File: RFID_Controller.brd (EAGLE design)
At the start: 77 x 67 mm, 25 parts, among them IC1 74HC595N, K1 FTR-K1C, T1 BC547, T2 BC547

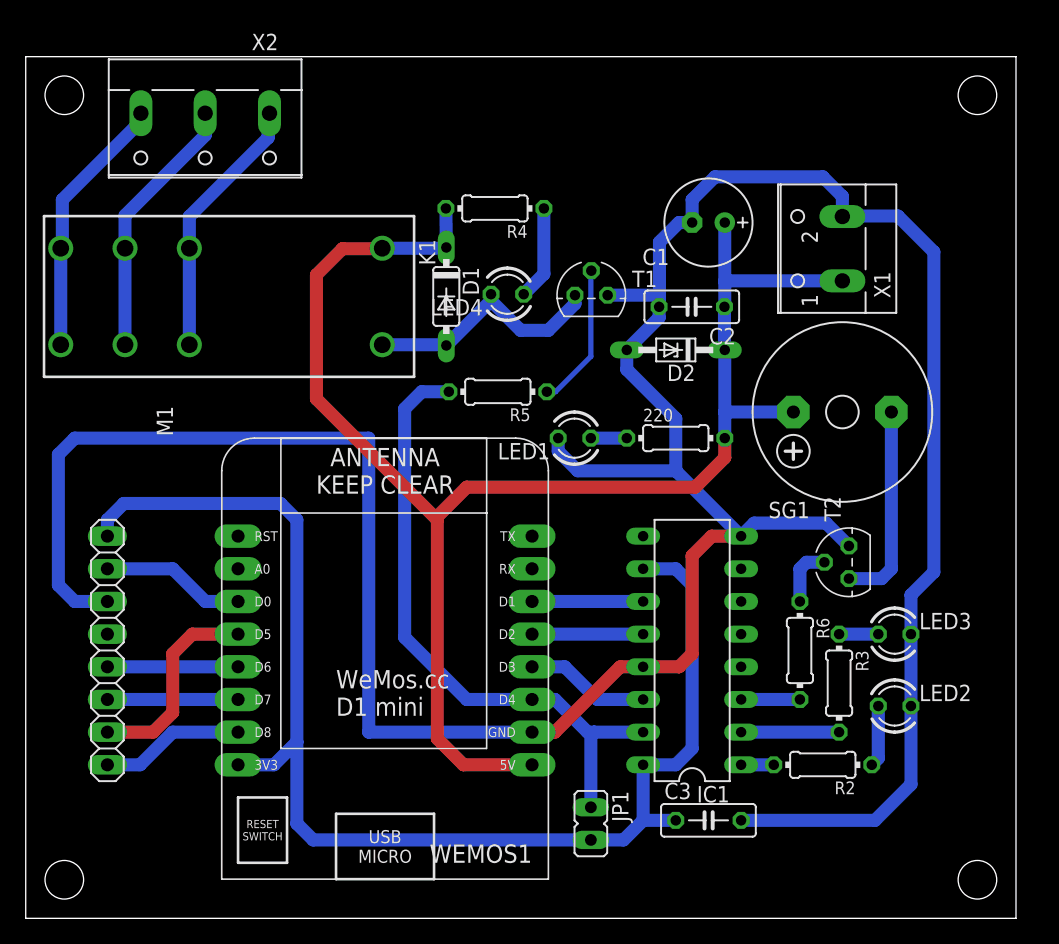
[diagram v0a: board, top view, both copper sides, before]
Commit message: -add: I2C Expander for more GPIOs -add: input for sabotage detection ( switch for enclosure cover ) -add: 2 more inputs for possible extensions -mod: additional resistor in pull-up path of relais transistor
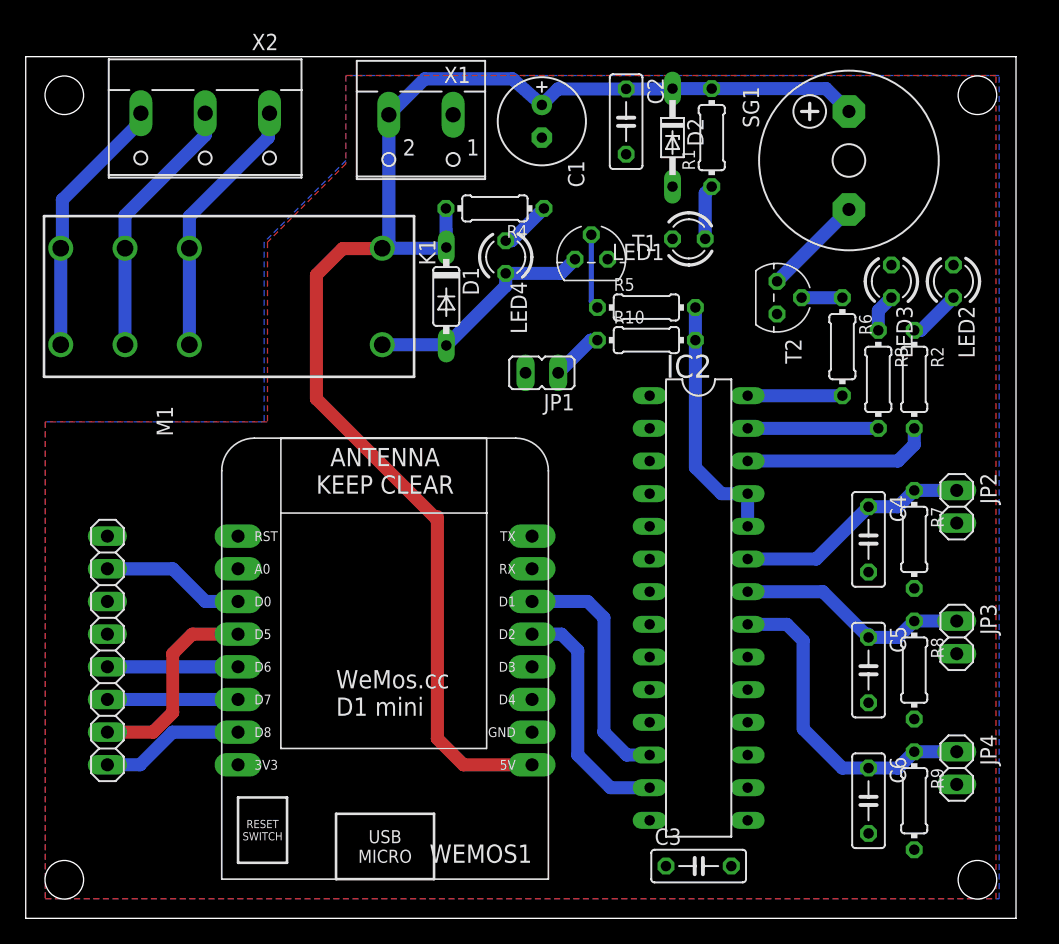
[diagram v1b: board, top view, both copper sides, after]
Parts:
- removed 220: (no value), rcl:0204/7
- removed IC1: 74HC595N, 74xx-eu:DIL16
- added C4, C5, C6: 100n, rcl:C050-025X075
- added IC2: MCP23017SP, microchip:DIL28-3
- added JP2, JP3, JP4: (no value), pinhead:1X02
- added R1: 220, rcl:0204/7
- added R10, R7, R8, R9: 10k, rcl:0204/7
- moved JP1 35.3 mm to (40.1, 42.4), turned to 90 degrees
- moved LED2 33.3 mm to (72.1, 49.5), turned to 270 degrees
- moved X1 32.8 mm to (30.7, 61.2), turned to 180 degrees
- moved R2 30.8 mm to (69.1, 41.9), turned to 270 degrees
- moved LED3 27.4 mm to (67.3, 49.5), turned to 270 degrees
- moved R6 23.9 mm to (63.5, 44.5)
- moved R3 23.8 mm to (66.3, 41.9)
- moved T2 21.3 mm to (58.4, 48.3), turned to 270 degrees
- moved SG1 19.6 mm to (64.0, 58.9), turned to 90 degrees
- moved LED1 17.9 mm to (51.6, 52.8)
- moved D2 16.5 mm to (50.3, 60.7), turned to 270 degrees
- moved C2 15.3 mm to (46.7, 62.0), turned to 270 degrees
- moved C1 15.2 mm to (40.1, 62.0), turned to 270 degrees
- moved R5 13.3 mm to (48.3, 47.5), turned to 0 degrees
- moved C3 3.64 mm to (52.3, 4.06)
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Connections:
- removed net CLK_595: IC1.11, WEMOS1.D1
- removed net SER: IC1.14, WEMOS1.D3
- removed net SET: IC1.12, WEMOS1.D2
- new net DK: C4.1, IC2.23, JP2.1, R7.1
- new net EX0: C5.1, IC2.22, JP3.1, R8.1
- new net EX1: C6.1, IC2.21, JP4.1, R9.1
- new net N$12: JP1.1, R10.1
- new net SCL: IC2.12, WEMOS1.D1
- new net SDA: IC2.13, WEMOS1.D2
- net 3V3: now also IC2.18, IC2.9, LED2.A, LED3.A, R7.2, R8.2, R9.2; no longer IC1.10, IC1.16
- net 5V: now also R1.2, X1.2; no longer 220.2, X1.1
- net BUZZ: now also IC2.28; no longer IC1.3
- net CONN: now also IC2.27; no longer IC1.2
- net GND: now also C4.2, C5.2, C6.2, IC2.10, IC2.15, IC2.16, IC2.17, JP2.2, JP3.2, JP4.2, X1.1; no longer IC1.13, IC1.8, LED2.K, LED3.K, X1.2
- net N$1: now also R1.1; no longer 220.1
- net N$2: now also LED2.K; no longer LED2.A
- net N$3: now also LED3.K; no longer LED3.A
- net SW: now also IC2.24, IC2.25, R10.2; no longer IC1.15, JP1.1, WEMOS1.D4
- net TXRX: now also IC2.26; no longer IC1.1
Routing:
- net GND: track 238.1 -> 0.00 mm
- net 3V3: track 102.3 -> 0.00 mm
- net SW: track 49.3 -> 19.9 mm
- net EX1: track 0.00 -> 25.4 mm
- net SCL: track 0.00 -> 19.3 mm
- net SDA: track 0.00 -> 18.9 mm
- net EX0: track 0.00 -> 18.5 mm
- net DK: track 0.00 -> 18.5 mm
- net TXRX: track 2.54 -> 14.8 mm
- net SER: track 9.69 -> 0.00 mm
- net SET: track 8.64 -> 0.00 mm
- net CLK_595: track 8.64 -> 0.00 mm
- net N$7: track 15.8 -> 7.90 mm
- net 5V: track 119.4 -> 112.0 mm
- net N$11: track 11.2 -> 5.85 mm
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- added copper zone on layer 1, net 3V3
- added copper zone on layer 16, net GND

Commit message: -mod: 2 additional Extra GPIO's -mod: replaced 3 single 1x2 pin headers with 2x5 pin header -mod: maximized copper area of relay contacts -info: Schematic verified by Ian Hubbertz
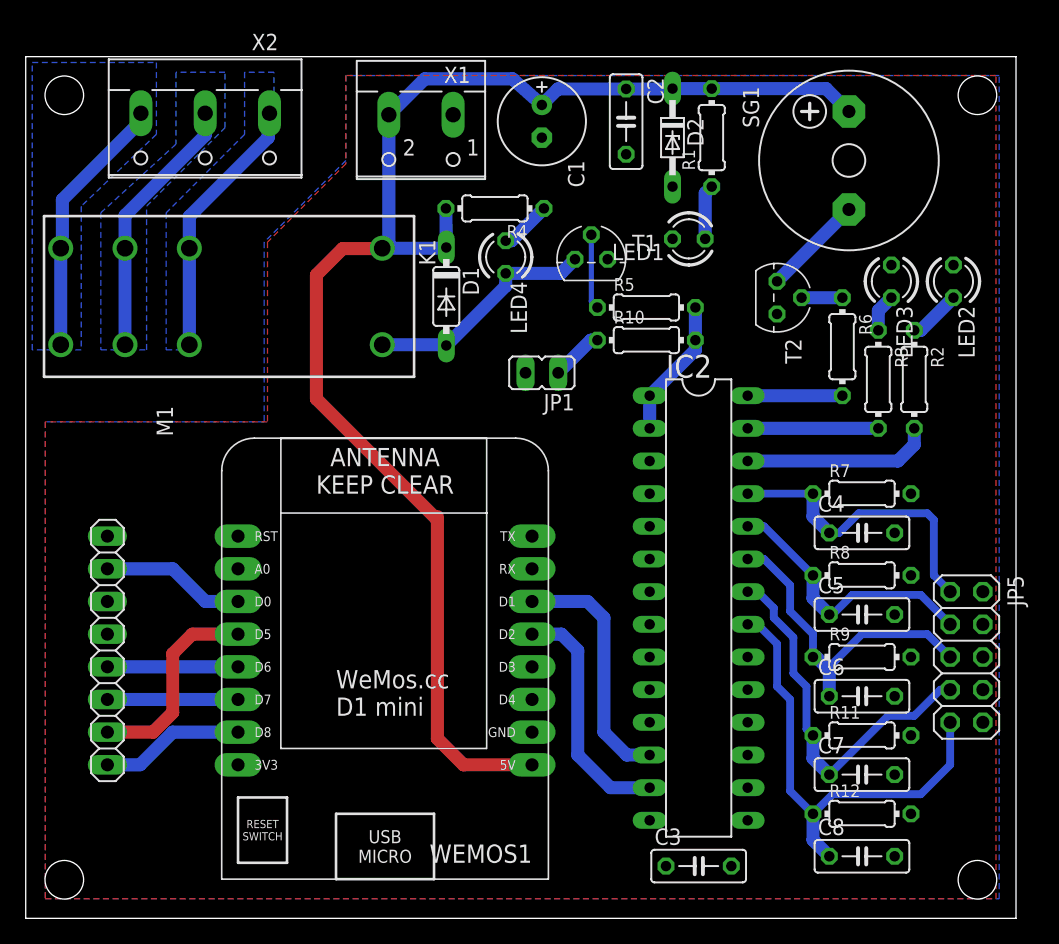
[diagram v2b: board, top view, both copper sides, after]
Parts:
- removed JP2, JP3, JP4: (no value), pinhead:1X02
- added C7, C8: 100n, rcl:C050-025X075
- added JP5: (no value), pinhead:2X05
- added R11, R12: 10k, rcl:0204/7
- moved R9 11.9 mm to (65.0, 20.3), turned to 0 degrees
- moved R8 8.41 mm to (65.0, 26.7), turned to 0 degrees
- moved C6 8.14 mm to (65.0, 17.3), turned to 0 degrees
- moved R7 5.40 mm to (65.0, 33.0), turned to 0 degrees
- moved C5 4.35 mm to (65.0, 23.6), turned to 0 degrees
- moved C4 0.72 mm to (65.0, 30.0), turned to 0 degrees
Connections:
- net N$10 renamed REL_NC
- net N$8 renamed REL_COMM
- net N$9 renamed REL_NO
- new net EX2: C7.1, IC2.22, JP5.7, R11.1
- new net EX3: C8.1, IC2.21, JP5.9, R12.1
- net 3V3: now also R11.2, R12.2
- net DK: now also IC2.25, JP5.1; no longer IC2.23, JP2.1
- net EX0: now also IC2.24, JP5.3; no longer IC2.22, JP3.1
- net EX1: now also IC2.23, JP5.5; no longer IC2.21, JP4.1
- net GND: now also C7.2, C8.2, JP5.10, JP5.2, JP5.4, JP5.6, JP5.8; no longer JP2.2, JP3.2, JP4.2
- net SW: now also IC2.1, IC2.2; no longer IC2.24, IC2.25
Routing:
- net EX3: track 0.00 -> 36.7 mm
- net EX2: track 0.00 -> 29.4 mm
- net SW: track 19.9 -> 10.9 mm
- net DK: track 18.5 -> 23.7 mm
- net EX0: track 18.5 -> 21.2 mm
- added copper zone on layer 16, net REL_COMM
- added copper zone on layer 16, net REL_NC
- added copper zone on layer 16, net REL_NO

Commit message: -mod: modifies according to Roberts recommendations
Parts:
- added C10, C9: 100p, rcl:C050-024X044
- added R13, R14: 1k, rcl:0204/7
- R10: value 10k -> 1k
- R2, R3: value 100 -> 100R
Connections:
- removed net N$11: R5.1, T1.2
- new net N$8: IC2.1, R5.2
- new net VCC: C9.1
- net 3V3: now also R13.1, R14.1
- net 5V: now also C10.1
- net GND: now also C10.2, C9.2
- net SCL: now also R13.2
- net SDA: now also R14.2
- net SW: now also R5.1, T1.2; no longer IC2.1, R5.2
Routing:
- net SW: track 10.9 -> 32.9 mm
- net 5V: track 112.0 -> 128.5 mm
- net N$8: track 0.00 -> 9.67 mm
- net N$11: track 5.85 -> 0.00 mm
- net SCL: track 19.3 -> 21.8 mm
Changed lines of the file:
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@@
 <grid distance="0.01" unitdist="inch" unit="inch" style="dots" multiple="1" display="yes" altdistance="0.01" altunitdist="inch" altunit="inch"/>
 <layers>
-<layer number="1" name="Top" color="4" fill="1" visible="no" active="yes"/>
-<layer number="16" name="Bottom" color="1" fill="1" visible="yes" active="yes"/>
+<layer number="1" name="Top" color="4" fill="1" visible="yes" active="yes"/>
+<layer number="16" name="Bottom" color="1" fill="1" visible="no" active="yes"/>
 <layer number="17" name="Pads" color="2" fill="1" visible="yes" active="yes"/>
 <layer number="18" name="Vias" color="2" fill="1" visible="yes" active="yes"/>
@@
 <element name="LED3" library="led" package="LED3MM" value="" x="67.31" y="49.53" rot="R270"/>
 <element name="LED4" library="led" package="LED3MM" value="" x="37.322" y="51.42" rot="R270"/>
-<element name="R2" library="rcl" package="0204/7" value="100" x="69.088" y="41.91" rot="R270"/>
-<element name="R3" library="rcl" package="0204/7" value="100" x="66.294" y="41.91" rot="R270"/>
+<element name="R2" library="rcl" package="0204/7" value="100R" x="69.088" y="41.91" rot="R270"/>
+<element name="R3" library="rcl" package="0204/7" value="100R" x="66.294" y="41.91" rot="R270"/>
 <element name="R4" library="rcl" package="0204/7" value="220" x="36.482" y="55.2" rot="R180"/>
 <element name="D1" library="diode" package="DO35-7" value="1N4148DO35-7" x="32.702" y="48.354" rot="R270"/>
@@
 <element name="C5" library="rcl" package="C050-025X075" value="100n" x="65.024" y="23.622"/>
 <element name="C6" library="rcl" package="C050-025X075" value="100n" x="65.024" y="17.272"/>
-<element name="R10" library="rcl" package="0204/7" value="10k" x="48.26" y="44.958"/>
+<element name="R10" library="rcl" package="0204/7" value="1k" x="48.26" y="44.958"/>
 <element name="JP5" library="pinhead" package="2X05" value="" x="73.152" y="20.32" rot="R270"/>
 <element name="R11" library="rcl" package="0204/7" value="10k" x="65.024" y="14.224"/>
@@
 <element name="C7" library="rcl" package="C050-025X075" value="100n" x="65.024" y="11.176"/>
 <element name="C8" library="rcl" package="C050-025X075" value="100n" x="65.024" y="4.826"/>
+<element name="R13" library="rcl" package="0204/7" value="1k" x="43.434" y="30.988" rot="R270"/>
+<element name="R14" library="rcl" package="0204/7" value="1k" x="45.466" y="6.35" rot="R90"/>
+<element name="C9" library="rcl" package="C050-024X044" value="100p" x="12.192" y="31.75" rot="R270"/>
+<element name="C10" library="rcl" package="C050-024X044" value="100p" x="42.418" y="6.35" rot="R270"/>
 </elements>
 <signals>
@@
 <vertex x="24.892" y="65.532"/>
 <vertex x="24.892" y="58.928"/>
-<vertex x="18.542" y="52.578"/>
+<vertex x="19.05" y="52.832"/>
+<vertex x="19.05" y="38.608"/>
+<vertex x="36.83" y="38.608"/>
+<vertex x="36.83" y="10.922"/>
+<vertex x="18.542" y="10.922"/>
 <vertex x="18.542" y="38.608"/>
 <vertex x="1.524" y="38.608"/>
@@
 <contactref element="JP5" pad="4"/>
 <contactref element="JP5" pad="10"/>
-</signal>
-<signal name="N$11">
-<contactref element="T1" pad="2"/>
-<contactref element="R5" pad="1"/>
-<wire x1="44.45" y1="47.498" x2="43.978" y2="47.97" width="0.4064" layer="16"/>
-<wire x1="43.978" y1="47.97" x2="43.978" y2="53.153" width="0.4064" layer="16"/>
+<contactref element="C10" pad="2"/>
+<contactref element="C9" pad="2"/>
 </signal>
 <signal name="5V">
@@
 <contactref element="R4" pad="2"/>
 <contactref element="SG1" pad="+"/>
-<wire x1="39.37" y1="11.938" x2="34.036" y2="11.938" width="1.016" layer="1"/>
-<wire x1="34.036" y1="11.938" x2="32.004" y2="13.97" width="1.016" layer="1"/>
-<wire x1="32.004" y1="13.97" x2="32.004" y2="30.988" width="1.016" layer="1"/>
-<wire x1="32.004" y1="30.988" x2="32.004" y2="31.242" width="1.016" layer="1"/>
 <wire x1="27.722" y1="52.104" x2="32.642" y2="52.104" width="1.016" layer="16"/>
 <wire x1="32.642" y1="52.104" x2="32.702" y2="52.164" width="1.016" layer="16"/>
@@
 <wire x1="27.688" y1="52.07" x2="24.638" y2="52.07" width="1.016" layer="1"/>
 <wire x1="24.638" y1="52.07" x2="22.606" y2="50.038" width="1.016" layer="1"/>
-<wire x1="22.606" y1="50.038" x2="22.606" y2="40.386" width="1.016" layer="1"/>
-<wire x1="22.606" y1="40.386" x2="32.004" y2="30.988" width="1.016" layer="1"/>
 <contactref element="C1" pad="+"/>
 <contactref element="X1" pad="2"/>
@@
 <wire x1="28.234" y1="52.616" x2="27.722" y2="52.104" width="1.016" layer="16"/>
 <wire x1="27.688" y1="52.07" x2="27.722" y2="52.104" width="1.016" layer="1"/>
+<contactref element="C10" pad="1"/>
+<wire x1="39.37" y1="11.938" x2="42.418" y2="8.89" width="1.016" layer="1"/>
+<wire x1="22.606" y1="50.038" x2="22.606" y2="45.72" width="1.016" layer="1"/>
+<wire x1="22.606" y1="45.72" x2="28.702" y2="39.624" width="1.016" layer="1"/>
+<wire x1="28.702" y1="39.624" x2="43.942" y2="39.624" width="1.016" layer="1"/>
+<wire x1="43.942" y1="39.624" x2="45.72" y2="37.846" width="1.016" layer="1"/>
+<wire x1="45.72" y1="37.846" x2="45.72" y2="26.162" width="1.016" layer="1"/>
+<wire x1="45.72" y1="26.162" x2="43.434" y2="23.876" width="1.016" layer="1"/>
+<wire x1="43.434" y1="23.876" x2="43.434" y2="13.716" width="1.016" layer="1"/>
+<wire x1="43.434" y1="13.716" x2="41.656" y2="11.938" width="1.016" layer="1"/>
+<wire x1="41.656" y1="11.938" x2="39.37" y2="11.938" width="1.016" layer="1"/>
 </signal>
 <signal name="3V3">
@@
 <vertex x="18.796" y="52.578"/>
 <vertex x="18.796" y="38.608"/>
+<vertex x="36.83" y="38.608"/>
+<vertex x="36.83" y="10.922"/>
+<vertex x="18.288" y="10.922"/>
+<vertex x="18.288" y="38.608"/>
 <vertex x="1.524" y="38.608"/>
 <vertex x="1.524" y="1.524"/>
@@
 <contactref element="R11" pad="2"/>
 <contactref element="R12" pad="2"/>
+<contactref element="R14" pad="1"/>
+<contactref element="R13" pad="1"/>
 </signal>
 <signal name="MISO">
@@
 </signal>
 <signal name="SW">
-<contactref element="R5" pad="2"/>
 <contactref element="R10" pad="2"/>
-<wire x1="52.07" y1="47.498" x2="52.07" y2="44.958" width="1.016" layer="16"/>
-<contactref element="IC2" pad="1"/>
 <contactref element="IC2" pad="2"/>
 <wire x1="52.07" y1="44.958" x2="52.07" y2="44.196" width="1.016" layer="16"/>
-<wire x1="52.07" y1="44.196" x2="48.514" y2="40.64" width="1.016" layer="16"/>
-<wire x1="48.514" y1="38.1" x2="48.514" y2="40.64" width="1.016" layer="16"/>
+<contactref element="R5" pad="1"/>
+<contactref element="T1" pad="2"/>
+<wire x1="44.45" y1="47.498" x2="43.978" y2="47.97" width="0.4064" layer="16"/>
+<wire x1="43.978" y1="47.97" x2="43.978" y2="53.153" width="0.4064" layer="16"/>
+<wire x1="48.514" y1="38.1" x2="50.546" y2="38.1" width="1.016" layer="16"/>
+<wire x1="50.546" y1="38.1" x2="52.07" y2="39.624" width="1.016" layer="16"/>
+<wire x1="52.07" y1="39.624" x2="52.07" y2="44.958" width="1.016" layer="16"/>
+<wire x1="44.45" y1="47.498" x2="45.72" y2="47.498" width="1.016" layer="16"/>
+<wire x1="45.72" y1="47.498" x2="47.752" y2="49.53" width="1.016" layer="16"/>
+<wire x1="47.752" y1="49.53" x2="53.594" y2="49.53" width="1.016" layer="16"/>
+<wire x1="53.594" y1="49.53" x2="54.61" y2="48.514" width="1.016" layer="16"/>
+<wire x1="54.61" y1="48.514" x2="54.61" y2="46.228" width="1.016" layer="16"/>
+<wire x1="54.61" y1="46.228" x2="53.34" y2="44.958" width="1.016" layer="16"/>
+<wire x1="53.34" y1="44.958" x2="52.07" y2="44.958" width="1.016" layer="16"/>
 </signal>
 <signal name="N$6">
@@
 <contactref element="IC2" pad="12"/>
 <contactref element="WEMOS1" pad="D1"/>
-<wire x1="39.37" y1="24.638" x2="43.688" y2="24.638" width="1.016" layer="16"/>
+<wire x1="39.37" y1="24.638" x2="43.434" y2="24.638" width="1.016" layer="16"/>
+<wire x1="43.434" y1="24.638" x2="43.688" y2="24.638" width="1.016" layer="16"/>
 <wire x1="43.688" y1="24.638" x2="44.958" y2="23.368" width="1.016" layer="16"/>
 <wire x1="44.958" y1="23.368" x2="44.958" y2="14.478" width="1.016" layer="16"/>
 <wire x1="44.958" y1="14.478" x2="46.736" y2="12.7" width="1.016" layer="16"/>
 <wire x1="46.736" y1="12.7" x2="48.514" y2="12.7" width="1.016" layer="16"/>
+<contactref element="R13" pad="2"/>
+<wire x1="43.434" y1="27.178" x2="43.434" y2="24.638" width="1.016" layer="16"/>
 </signal>
 <signal name="SDA">
@@
 <wire x1="42.926" y1="12.7" x2="45.466" y2="10.16" width="1.016" layer="16"/>
 <wire x1="45.466" y1="10.16" x2="48.514" y2="10.16" width="1.016" layer="16"/>
+<contactref element="R14" pad="2"/>
 </signal>
 <signal name="DK">
@@
 <wire x1="69.596" y1="9.652" x2="62.738" y2="9.652" width="0.6096" layer="16"/>
 </signal>
+<signal name="N$8">
+<contactref element="R5" pad="2"/>
+<contactref element="IC2" pad="1"/>
+<wire x1="48.514" y1="40.64" x2="48.514" y2="46.228" width="1.016" layer="16"/>
+<wire x1="48.514" y1="46.228" x2="49.784" y2="47.498" width="1.016" layer="16"/>
+<wire x1="49.784" y1="47.498" x2="52.07" y2="47.498" width="1.016" layer="16"/>
+</signal>
+<signal name="VCC">
+<contactref element="C9" pad="1"/>
+</signal>
 </signals>
